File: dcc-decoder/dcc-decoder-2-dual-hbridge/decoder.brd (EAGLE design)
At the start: 98.8 x 80 mm, 30 parts, among them U4 ATMEGA328P, U5 MPC17531-ES, Y1 16MHZ

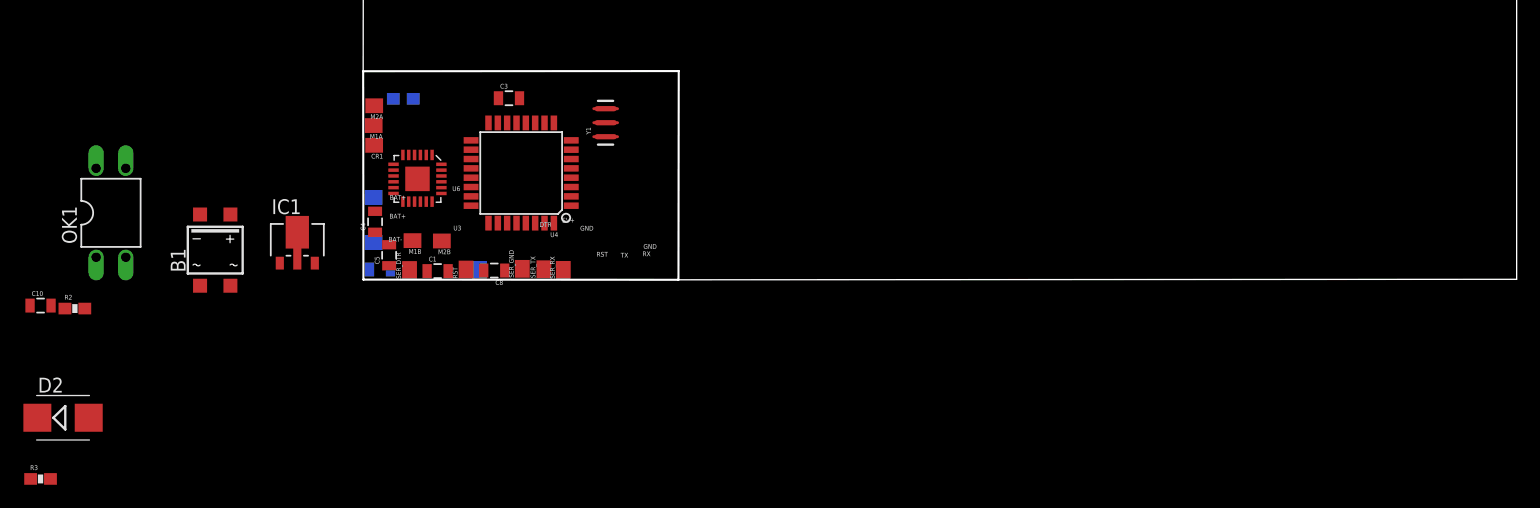
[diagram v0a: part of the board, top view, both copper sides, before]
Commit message: New layout for RFM69HC
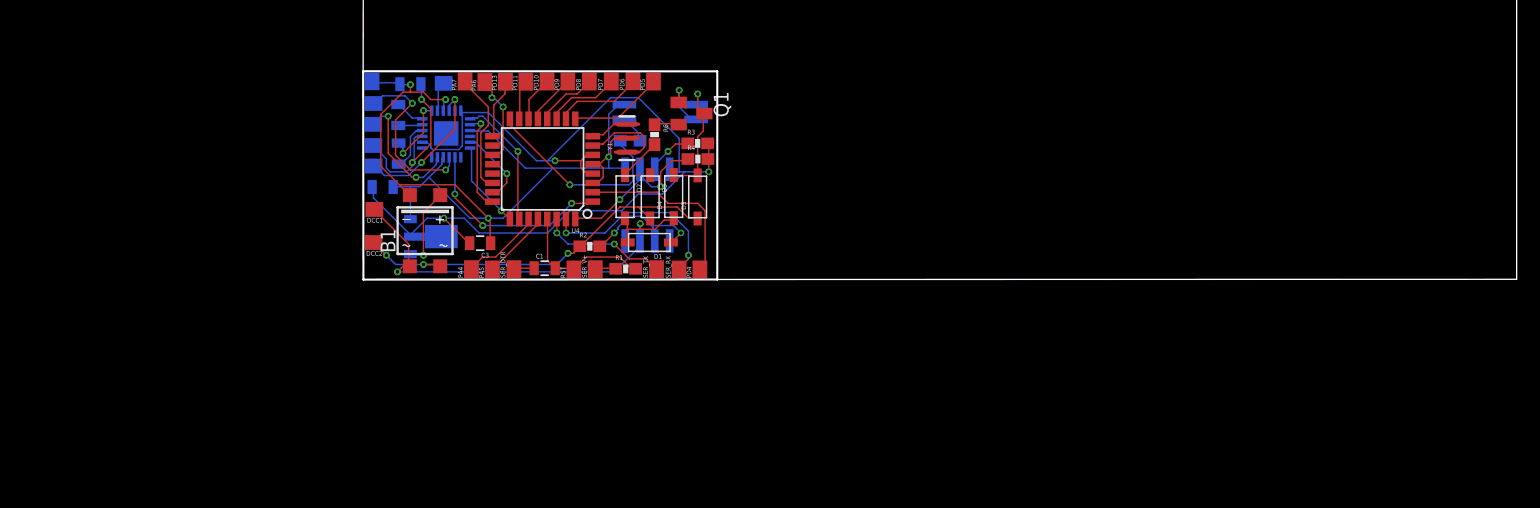
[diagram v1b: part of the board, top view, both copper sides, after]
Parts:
- removed C10: 4.7uF, SparkFun-Capacitors:0805
- removed OK1: PC817, optocoupler:DIL04
- added D1, D3, D4, D5: 11n4148, adafruit:SOD-123
- added OK2: PC817SOP4, optocoupler:SOP4
- added OK3: 6N137SOP8, optocoupler:SOIC08
- added PA4, PA5, PA6, PA7, PD10, PD11, PD13, PD4, PD5, PD6, PD7, PD8, PD9: (no value), wirepad:SMD1,27-2,54
- added Q1: BC858ASMD, transistor-pnp:SOT23-BEC
- added R4: 10k, SparkFun-Resistors:0603-RES
- added R5: 1k, SparkFun-Resistors:0603-RES
- added R6: 100, SparkFun-Resistors:0603-RES
- D2: value ES2D -> 11n4148; device diode:SMB -> adafruit:SOD-123
- IC1: value (none) -> 78L05
- R2: value 10k -> 1k5
- moved R3 63.2 mm to (29.8, 11.6)
- moved D2 51.7 mm to (23.6, 7.08), turned to 270 degrees
- moved R2 44.4 mm to (20.6, 2.83)
- moved R1 24.0 mm to (23.7, 0.89), flipped to the top, turned to 0 degrees
- moved SER_GND 20.6 mm to (1.94, 17.0), flipped to the bottom
- moved B1 18.1 mm to (6.49, 4.16)
- moved C8 17.5 mm to (5.24, 16.7), flipped to the bottom
- moved M1B 13.7 mm to (8.08, 16.8), flipped to the bottom
- moved C3 12.7 mm to (11.2, 3.09), turned to 180 degrees
- moved IC1 11.4 mm to (6.98, 3.65), flipped to the bottom, turned to 90 degrees
- moved SER_V+ 9.92 mm to (21.1, 0.87), flipped to the top
- moved SER_RX 9.92 mm to (28.2, 0.84)
- moved SER_TX 9.65 mm to (26.3, 0.87)
- moved C4 9.36 mm to (4.19, 14.1), flipped to the bottom, turned to 270 degrees
- moved RST 9.24 mm to (19.2, 0.85)
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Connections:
- removed net MISO: U4.16
- removed net MOSI: U4.15
- removed net N$11: B1.~1, C10.2, D2.A, DCC1.1, OK1.2
- removed net N$22: B1.~2, DCC2.1, R2.1
- removed net SCK: U4.17
- removed net SS: U4.14
- new net D10: PD10.1, U4.14
- new net D11: PD11.1, U4.15
- new net D12: R5.1, U4.16
- new net D13: PD13.1, U4.17
- new net D8: PD8.1, U4.12
- new net D9: PD9.1, U4.13
- new net DCC1: B1.~1, D1.A, D2.A, D4.C, DCC1.1, OK3.3
- new net DCC2: B1.~2, D3.A, D5.C, DCC2.1, R2.1
- new net N$13: OK3.7, R3.1
- new net N$16: OK2.1, R5.2
- new net N$18: OK2.4, Q1.B
- new net N$19: D4.A, D5.A, OK2.3, Q1.C
- new net N$21: Q1.E, R6.1
- new net N$24: D2.C, D3.C, R6.2
- net A4: now also PA4.1
- net A5: now also PA5.1
- net A6: now also PA6.1
- net A7: now also PA7.1
- net D2: now also OK3.6, R4.1; no longer OK1.4, R3.1
- net D4: now also PD4.1
- net D5: now also PD5.1
- net D6: now also PD6.1
- net D7: now also PD7.1
- net GND: now also OK2.2, OK3.5; no longer OK1.3
- net N$8: now also D1.C, OK3.2; no longer C10.1, D2.C, OK1.1
- net VCC: now also OK3.8, R4.2
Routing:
- net VCC: track 0.00 -> 82.1 mm, vias 0 -> 3
- net GND: track 0.00 -> 80.4 mm, vias 0 -> 4
- net DCC1: track 0.00 -> 38.7 mm, vias 0 -> 2
- net DCC2: track 0.00 -> 34.0 mm, vias 0 -> 3
- net D12: track 0.00 -> 17.2 mm, vias 0 -> 1
- net D3: track 0.00 -> 17.1 mm, vias 0 -> 3
- net TX: track 0.00 -> 16.7 mm, vias 0 -> 2
- net N$20: track 0.00 -> 16.0 mm, vias 0 -> 2
- net D4: track 0.00 -> 15.5 mm
- net N$14: track 0.00 -> 14.9 mm, vias 0 -> 2
- net D2: track 0.00 -> 14.7 mm, vias 0 -> 2
- net N$17: track 0.00 -> 12.7 mm, vias 0 -> 2
- net N$5: track 0.00 -> 12.3 mm
- net N$8: track 0.00 -> 11.4 mm, vias 0 -> 2
- net A3: track 0.00 -> 11.3 mm, vias 0 -> 1
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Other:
- outline, holes or cut-outs redrawn
- board text removed: "3.3"
- board text removed: "BAT+"
- board text removed: "BAT-"
- board text removed: "DTR"
- board text removed: "GND"
- board text removed: "RST"
- board text removed: "RX"
- board text removed: "SV+"
- board text removed: "TX"
- board text removed: "U3"
- board text removed: "U6"
- board text removed: "gnd"
- board text removed: "hss"
- board text removed: "rst"
- board text removed: "sck"
- board text removed: "si"
- board text removed: "so"
